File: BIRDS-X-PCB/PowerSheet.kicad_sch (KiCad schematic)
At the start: 0 parts

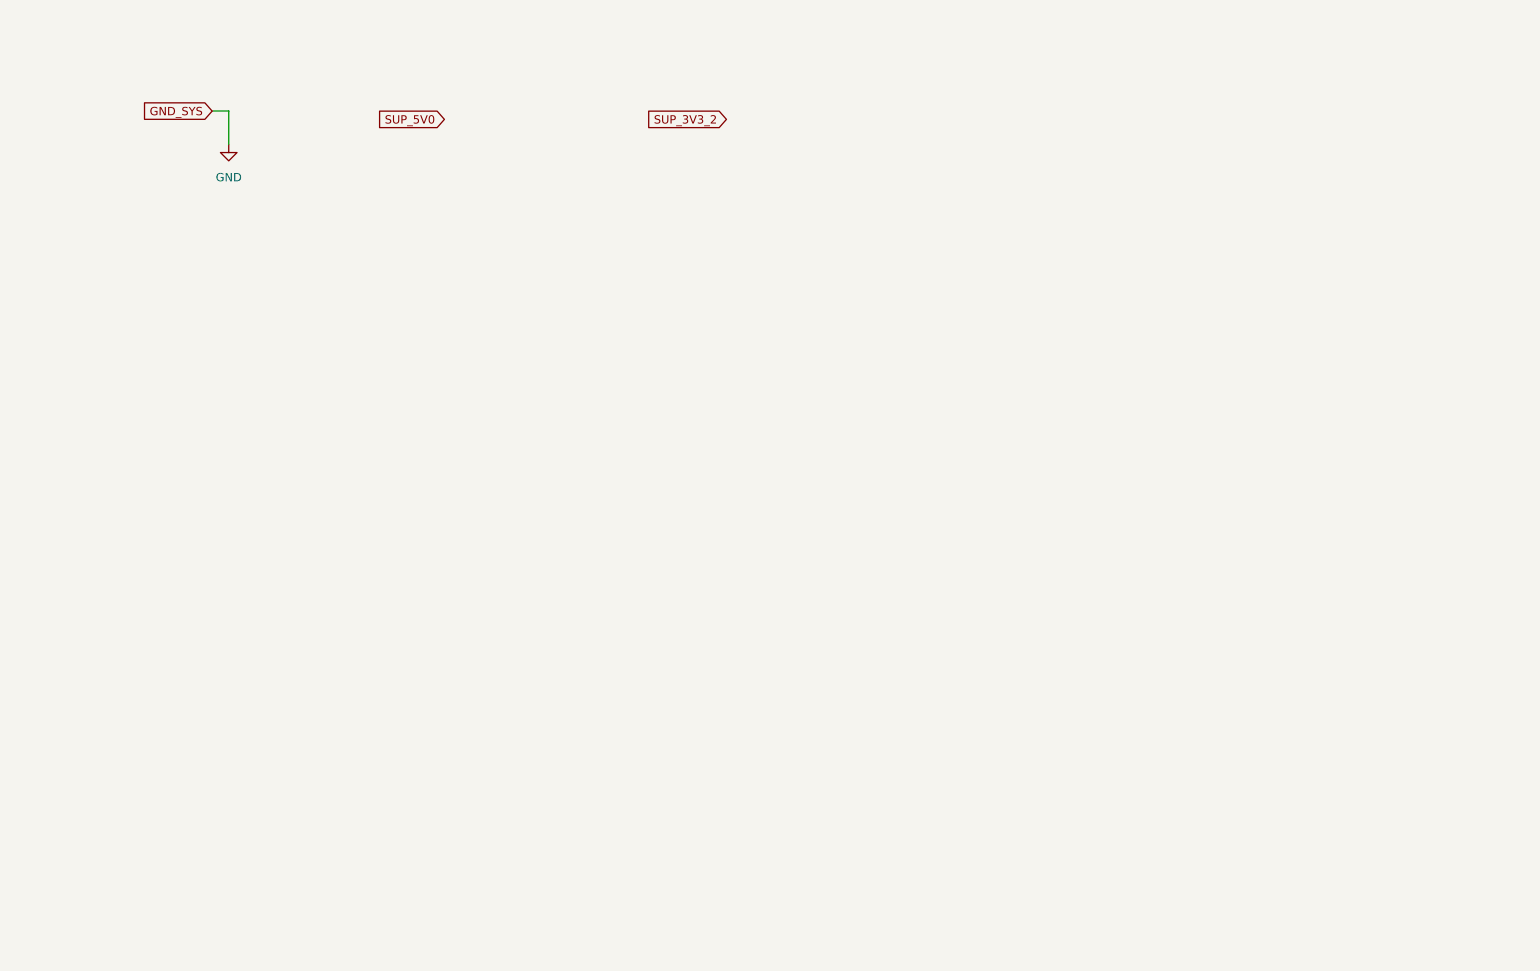
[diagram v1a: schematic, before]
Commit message: Finish power OCP
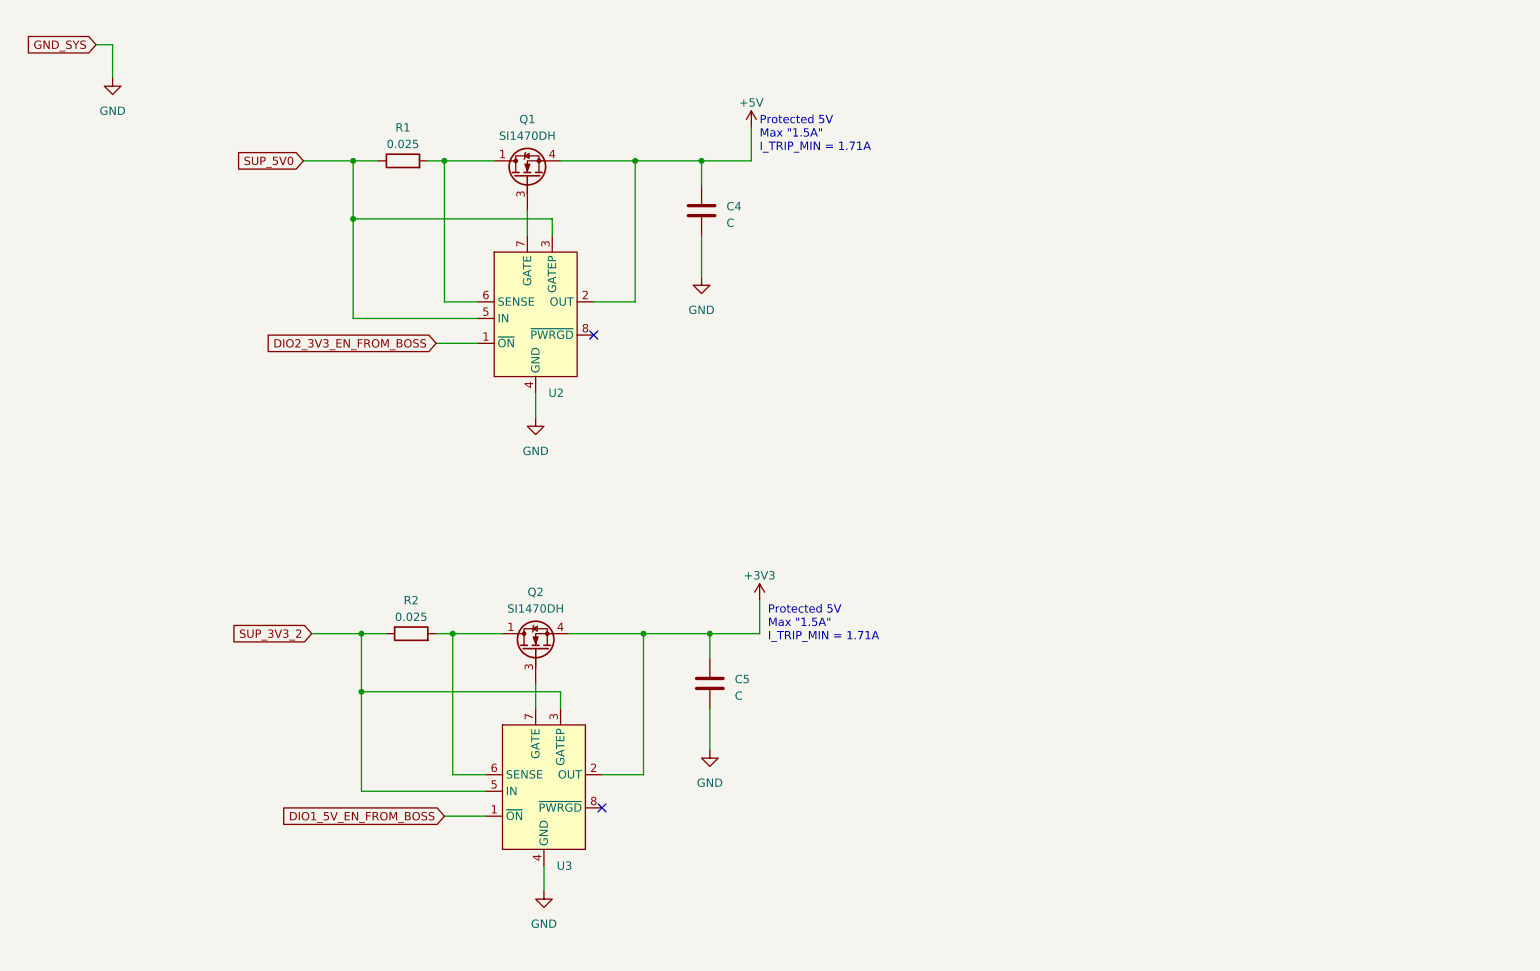
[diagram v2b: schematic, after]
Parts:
- added C4, C5: C, symbol Device:C
- added Q1, Q2: SI1470DH, Package_TO_SOT_SMD:SOT-363_SC-70-6, symbol Transistor_FET:Si1442DH
- added R1, R2: 0.025, symbol Device:R
- added U2, U3: ~, Package_TO_SOT_SMD:TSOT-23-8_HandSoldering, symbol BIRDS-X_Symbols_Lib:LTC4361-X_TS8
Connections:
- net GND: now also C4.2, C5.2, U2.4 (GND), U3.4 (GND)
- net SUP_3V3_2: now also R2.1, U3.3 (GATEP), U3.5 (IN)
- net SUP_5V0: now also R1.1, U2.3 (GATEP), U2.5 (IN)
- new net: Q2.1 (D), Q2.2 (D), Q2.5 (D), Q2.6 (D), R2.2, U3.6 (SENSE)
- new net: Q2.3 (G), U3.7 (GATE)
- new net: Q1.1 (D), Q1.2 (D), Q1.5 (D), Q1.6 (D), R1.2, U2.6 (SENSE)
- new net: Q1.3 (G), U2.7 (GATE)
- new net +3V3: C5.1, Q2.4 (S), U3.2 (OUT)
- new net +5V: C4.1, Q1.4 (S), U2.2 (OUT)
- new net DIO1_5V_EN_FROM_BOSS: U3.1 (~{ON})
- new net DIO2_3V3_EN_FROM_BOSS: U2.1 (~{ON})
- no-connect marks 0 -> 2
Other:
- note added: "Protected 5V Max "1.5A" I_TRIP_MIN = 1.71A"

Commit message: Add BOM and footprints
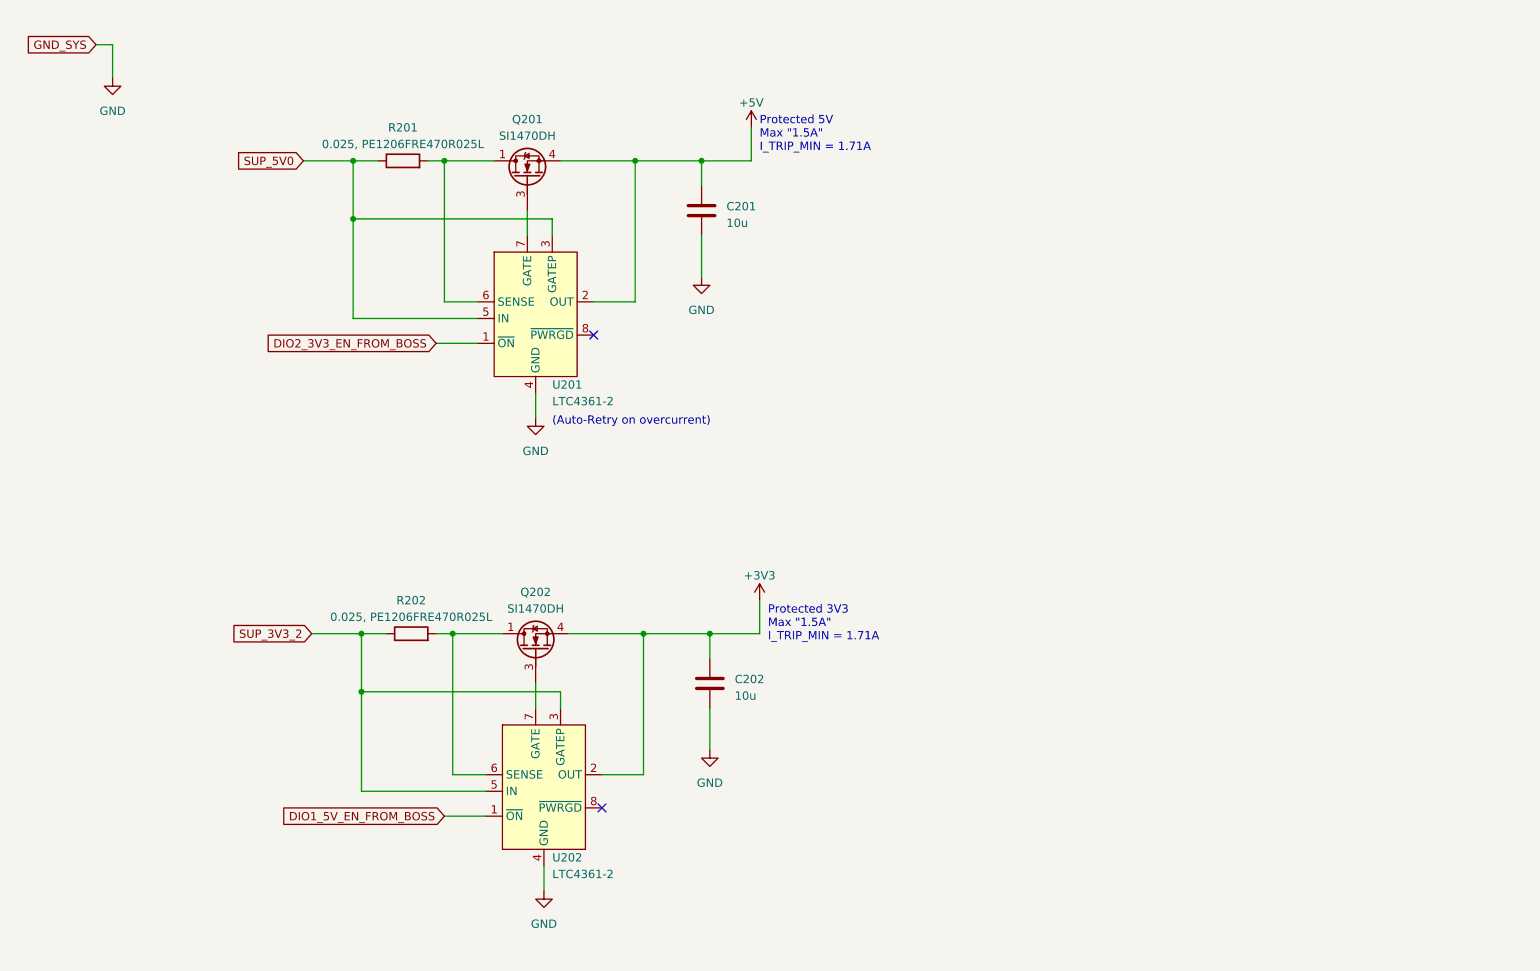
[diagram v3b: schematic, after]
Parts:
- C201: renamed from C4; value C -> 10u; footprint (none) -> Capacitor_SMD:C_1206_3216Metric_Pad1.33x1.80mm_HandSolder
- C202: renamed from C5; value C -> 10u; footprint (none) -> Capacitor_SMD:C_1206_3216Metric_Pad1.33x1.80mm_HandSolder
- R201: renamed from R1; value 0.025 -> 0.025, PE1206FRE470R025L; footprint (none) -> Resistor_SMD:R_1206_3216Metric_Pad1.30x1.75mm_HandSolder
- R202: renamed from R2; value 0.025 -> 0.025, PE1206FRE470R025L; footprint (none) -> Resistor_SMD:R_1206_3216Metric_Pad1.30x1.75mm_HandSolder
- U201: renamed from U2; value ~ -> LTC4361-2
- U202: renamed from U3; value ~ -> LTC4361-2
- renumbered Q1 to Q201, Q2 to Q202
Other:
- note added: "(Auto-Retry on overcurrent)"
- note added: "Protected 3V3 Max "1.5A" I_TRIP_MIN = 1.71A"
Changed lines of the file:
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@@
     (effects (font (size 1.27 1.27)) (justify left bottom))
   )
-  (text "Protected 5V\nMax \"1.5A\"\nI_TRIP_MIN = 1.71A" (at 132.08 115.57 0)
+  (text "(Auto-Retry on overcurrent)" (at 99.06 82.55 0)
+    (effects (font (size 1.27 1.27)) (justify left bottom))
+  )
+  (text "Protected 3V3\nMax \"1.5A\"\nI_TRIP_MIN = 1.71A" (at 132.08 115.57 0)
     (effects (font (size 1.27 1.27)) (justify left bottom))
   )
@@
   (symbol (lib_id "power:+5V") (at 129.54 36.83 0) (unit 1)
     (in_bom yes) (on_board yes) (dnp no) (fields_autoplaced)
-    (property "Reference" "#PWR010" (at 129.54 40.64 0)
+    (property "Reference" "#PWR0206" (at 129.54 40.64 0)
       (effects (font (size 1.27 1.27)) hide)
     )
@@
       (project "BIRDS-X-PCB"
         (path "/c2796b15-795a-4d6e-ad4b-0ba87ded4bc9/f0b1214b-f453-423f-b2cf-f5d10e08eafe"
-          (reference "#PWR010") (unit 1)
+          (reference "#PWR0206") (unit 1)
         )
       )
@@
         )
         (path "/c2796b15-795a-4d6e-ad4b-0ba87ded4bc9/f0b1214b-f453-423f-b2cf-f5d10e08eafe"
-          (reference "#PWR011") (unit 1)
+          (reference "#PWR0204") (unit 1)
         )
       )
@@
   (symbol (lib_id "Device:C") (at 121.92 49.53 0) (unit 1)
     (in_bom yes) (on_board yes) (dnp no) (fields_autoplaced)
-    (property "Reference" "C4" (at 125.73 48.895 0)
-      (effects (font (size 1.27 1.27)) (justify left))
-    )
-    (property "Value" "C" (at 125.73 51.435 0)
-      (effects (font (size 1.27 1.27)) (justify left))
-    )
-    (property "Footprint" "" (at 122.8852 53.34 0)
+    (property "Reference" "C201" (at 125.73 48.895 0)
+      (effects (font (size 1.27 1.27)) (justify left))
+    )
+    (property "Value" "10u" (at 125.73 51.435 0)
+      (effects (font (size 1.27 1.27)) (justify left))
+    )
+    (property "Footprint" "Capacitor_SMD:C_1206_3216Metric_Pad1.33x1.80mm_HandSolder" (at 122.8852 53.34 0)
       (effects (font (size 1.27 1.27)) hide)
     )
@@
       (project "BIRDS-X-PCB"
         (path "/c2796b15-795a-4d6e-ad4b-0ba87ded4bc9/f0b1214b-f453-423f-b2cf-f5d10e08eafe"
-          (reference "C4") (unit 1)
+          (reference "C201") (unit 1)
         )
       )
@@
   (symbol (lib_id "Transistor_FET:Si1442DH") (at 96.52 116.84 90) (unit 1)
     (in_bom yes) (on_board yes) (dnp no) (fields_autoplaced)
-    (property "Reference" "Q2" (at 96.52 107.95 90)
+    (property "Reference" "Q202" (at 96.52 107.95 90)
       (effects (font (size 1.27 1.27)))
     )
@@
       (project "BIRDS-X-PCB"
         (path "/c2796b15-795a-4d6e-ad4b-0ba87ded4bc9/f0b1214b-f453-423f-b2cf-f5d10e08eafe"
-          (reference "Q2") (unit 1)
+          (reference "Q202") (unit 1)
         )
       )
@@
   )
   (symbol (lib_id "BIRDS-X_Symbols_Lib:LTC4361-X_TS8") (at 96.52 62.23 0) (unit 1)
-    (in_bom yes) (on_board yes) (dnp no) (fields_autoplaced)
-    (property "Reference" "U2" (at 98.4759 77.47 0)
-      (effects (font (size 1.27 1.27)) (justify left))
-    )
-    (property "Value" "~" (at 96.52 62.23 0)
-      (effects (font (size 1.27 1.27)))
+    (in_bom yes) (on_board yes) (dnp no)
+    (property "Reference" "U201" (at 99.06 76.2 0)
+      (effects (font (size 1.27 1.27)) (justify left))
+    )
+    (property "Value" "LTC4361-2" (at 99.06 78.74 0)
+      (effects (font (size 1.27 1.27)) (justify left))
     )
     (property "Footprint" "Package_TO_SOT_SMD:TSOT-23-8_HandSoldering" (at 97.79 92.71 0)
@@
       (project "BIRDS-X-PCB"
         (path "/c2796b15-795a-4d6e-ad4b-0ba87ded4bc9/f0b1214b-f453-423f-b2cf-f5d10e08eafe"
-          (reference "U2") (unit 1)
+          (reference "U201") (unit 1)
         )
       )
@@
         )
         (path "/c2796b15-795a-4d6e-ad4b-0ba87ded4bc9/f0b1214b-f453-423f-b2cf-f5d10e08eafe"
-          (reference "#PWR012") (unit 1)
+          (reference "#PWR0203") (unit 1)
         )
       )
@@
         )
         (path "/c2796b15-795a-4d6e-ad4b-0ba87ded4bc9/f0b1214b-f453-423f-b2cf-f5d10e08eafe"
-          (reference "#PWR013") (unit 1)
+          (reference "#PWR0205") (unit 1)
         )
       )
@@
   (symbol (lib_id "power:+3V3") (at 130.81 109.22 0) (unit 1)
     (in_bom yes) (on_board yes) (dnp no) (fields_autoplaced)
-    (property "Reference" "#PWR014" (at 130.81 113.03 0)
+    (property "Reference" "#PWR0207" (at 130.81 113.03 0)
       (effects (font (size 1.27 1.27)) hide)
     )
@@
       (project "BIRDS-X-PCB"
         (path "/c2796b15-795a-4d6e-ad4b-0ba87ded4bc9/f0b1214b-f453-423f-b2cf-f5d10e08eafe"
-          (reference "#PWR014") (unit 1)
+          (reference "#PWR0207") (unit 1)
         )
       )
@@
   (symbol (lib_id "Device:R") (at 76.2 41.91 90) (unit 1)
     (in_bom yes) (on_board yes) (dnp no) (fields_autoplaced)
-    (property "Reference" "R1" (at 76.2 36.83 90)
-      (effects (font (size 1.27 1.27)))
-    )
-    (property "Value" "0.025" (at 76.2 39.37 90)
-      (effects (font (size 1.27 1.27)))
-    )
-    (property "Footprint" "" (at 76.2 43.688 90)
+    (property "Reference" "R201" (at 76.2 36.83 90)
+      (effects (font (size 1.27 1.27)))
+    )
+    (property "Value" "0.025, PE1206FRE470R025L" (at 76.2 39.37 90)
+      (effects (font (size 1.27 1.27)))
+    )
+    (property "Footprint" "Resistor_SMD:R_1206_3216Metric_Pad1.30x1.75mm_HandSolder" (at 76.2 43.688 90)
       (effects (font (size 1.27 1.27)) hide)
     )
@@
       (project "BIRDS-X-PCB"
         (path "/c2796b15-795a-4d6e-ad4b-0ba87ded4bc9/f0b1214b-f453-423f-b2cf-f5d10e08eafe"
-          (reference "R1") (unit 1)
+          (reference "R201") (unit 1)
         )
       )
@@
   (symbol (lib_id "Device:C") (at 123.19 121.92 0) (unit 1)
     (in_bom yes) (on_board yes) (dnp no) (fields_autoplaced)
-    (property "Reference" "C5" (at 127 121.285 0)
-      (effects (font (size 1.27 1.27)) (justify left))
-    )
-    (property "Value" "C" (at 127 123.825 0)
-      (effects (font (size 1.27 1.27)) (justify left))
-    )
-    (property "Footprint" "" (at 124.1552 125.73 0)
+    (property "Reference" "C202" (at 127 121.285 0)
+      (effects (font (size 1.27 1.27)) (justify left))
+    )
+    (property "Value" "10u" (at 127 123.825 0)
+      (effects (font (size 1.27 1.27)) (justify left))
+    )
+    (property "Footprint" "Capacitor_SMD:C_1206_3216Metric_Pad1.33x1.80mm_HandSolder" (at 124.1552 125.73 0)
       (effects (font (size 1.27 1.27)) hide)
     )
@@
       (project "BIRDS-X-PCB"
         (path "/c2796b15-795a-4d6e-ad4b-0ba87ded4bc9/f0b1214b-f453-423f-b2cf-f5d10e08eafe"
-          (reference "C5") (unit 1)
+          (reference "C202") (unit 1)
         )
       )
@@
   (symbol (lib_id "Transistor_FET:Si1442DH") (at 95.25 44.45 90) (unit 1)
     (in_bom yes) (on_board yes) (dnp no) (fields_autoplaced)
-    (property "Reference" "Q1" (at 95.25 35.56 90)
+    (property "Reference" "Q201" (at 95.25 35.56 90)
       (effects (font (size 1.27 1.27)))
     )
@@
       (project "BIRDS-X-PCB"
         (path "/c2796b15-795a-4d6e-ad4b-0ba87ded4bc9/f0b1214b-f453-423f-b2cf-f5d10e08eafe"
-          (reference "Q1") (unit 1)
+          (reference "Q201") (unit 1)
         )
       )
@@
         )
         (path "/c2796b15-795a-4d6e-ad4b-0ba87ded4bc9/f0b1214b-f453-423f-b2cf-f5d10e08eafe"
-          (reference "#PWR08") (unit 1)
+          (reference "#PWR0201") (unit 1)
         )
       )
@@
   (symbol (lib_id "Device:R") (at 77.47 114.3 90) (unit 1)
     (in_bom yes) (on_board yes) (dnp no) (fields_autoplaced)
-    (property "Reference" "R2" (at 77.47 109.22 90)
-      (effects (font (size 1.27 1.27)))
-    )
-    (property "Value" "0.025" (at 77.47 111.76 90)
-      (effects (font (size 1.27 1.27)))
-    )
-    (property "Footprint" "" (at 77.47 116.078 90)
+    (property "Reference" "R202" (at 77.47 109.22 90)
+      (effects (font (size 1.27 1.27)))
+    )
+    (property "Value" "0.025, PE1206FRE470R025L" (at 77.47 111.76 90)
+      (effects (font (size 1.27 1.27)))
+    )
+    (property "Footprint" "Resistor_SMD:R_1206_3216Metric_Pad1.30x1.75mm_HandSolder" (at 77.47 116.078 90)
       (effects (font (size 1.27 1.27)) hide)
     )
@@
       (project "BIRDS-X-PCB"
         (path "/c2796b15-795a-4d6e-ad4b-0ba87ded4bc9/f0b1214b-f453-423f-b2cf-f5d10e08eafe"
-          (reference "R2") (unit 1)
+          (reference "R202") (unit 1)
         )
       )
@@
         )
         (path "/c2796b15-795a-4d6e-ad4b-0ba87ded4bc9/f0b1214b-f453-423f-b2cf-f5d10e08eafe"
-          (reference "#PWR09") (unit 1)
+          (reference "#PWR0202") (unit 1)
         )
       )
@@
   )
   (symbol (lib_id "BIRDS-X_Symbols_Lib:LTC4361-X_TS8") (at 97.79 134.62 0) (unit 1)
-    (in_bom yes) (on_board yes) (dnp no) (fields_autoplaced)
-    (property "Reference" "U3" (at 99.7459 149.86 0)
-      (effects (font (size 1.27 1.27)) (justify left))
-    )
-    (property "Value" "~" (at 97.79 134.62 0)
-      (effects (font (size 1.27 1.27)))
+    (in_bom yes) (on_board yes) (dnp no)
+    (property "Reference" "U202" (at 99.06 148.59 0)
+      (effects (font (size 1.27 1.27)) (justify left))
+    )
+    (property "Value" "LTC4361-2" (at 99.06 151.13 0)
+      (effects (font (size 1.27 1.27)) (justify left))
     )
     (property "Footprint" "Package_TO_SOT_SMD:TSOT-23-8_HandSoldering" (at 99.06 165.1 0)
@@
       (project "BIRDS-X-PCB"
         (path "/c2796b15-795a-4d6e-ad4b-0ba87ded4bc9/f0b1214b-f453-423f-b2cf-f5d10e08eafe"
-          (reference "U3") (unit 1)
-        )
-      )
+          (reference "U202") (unit 1)
+        )
+      )
